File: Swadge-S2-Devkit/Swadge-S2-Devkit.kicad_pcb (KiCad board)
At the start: 2 copper layers, 99.9 x 99.9 mm, 72 parts, among them J1 USB_B_Micro, M1 Motor_DC, Q1 Q_NPN_BEC, Q2 Q_NPN_BEC, SW1 4-1437565-2, SW10 4-1437565-2, SW11 4-1437565-2, SW12 4-1437565-2, SW13 touch-ring-6, SW14 SW_SPDT, SW2 4-1437565-2, SW3 4-1437565-2, SW4 4-1437565-2, SW5 4-1437565-2, SW6 4-1437565-2, SW7 4-1437565-2, SW8 4-1437565-2, SW9 4-1437565-2, U1 ESP32-S2-SOLO, U2 BUS_PCIexpress, U3 AP1117-33, U4 GS321-TR, U5 QMA7981, U6 INGHAi_GSPK2308P-8R0.5W, U7 TFT-1.14, U8 TFT_DISPLAY

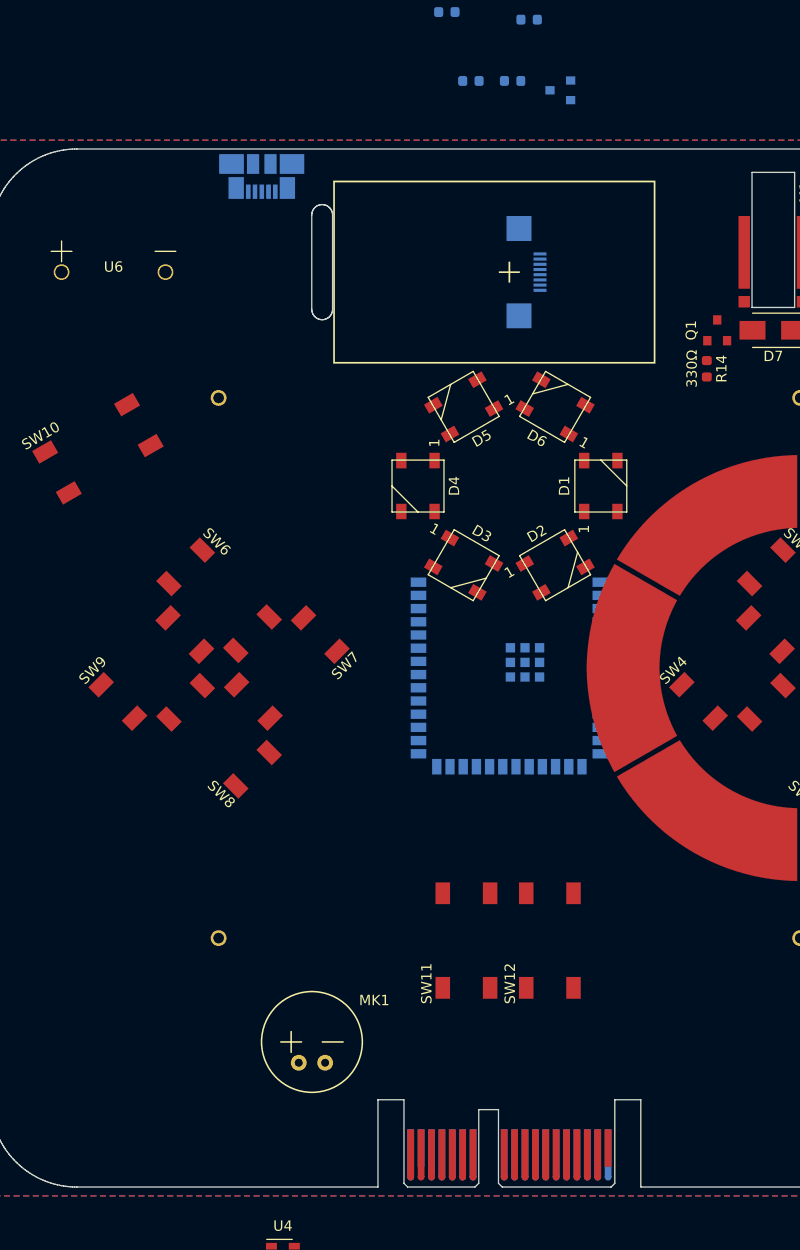
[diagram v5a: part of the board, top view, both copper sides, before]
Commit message: Added diodes to USB, added pin headers, cleaned schematic
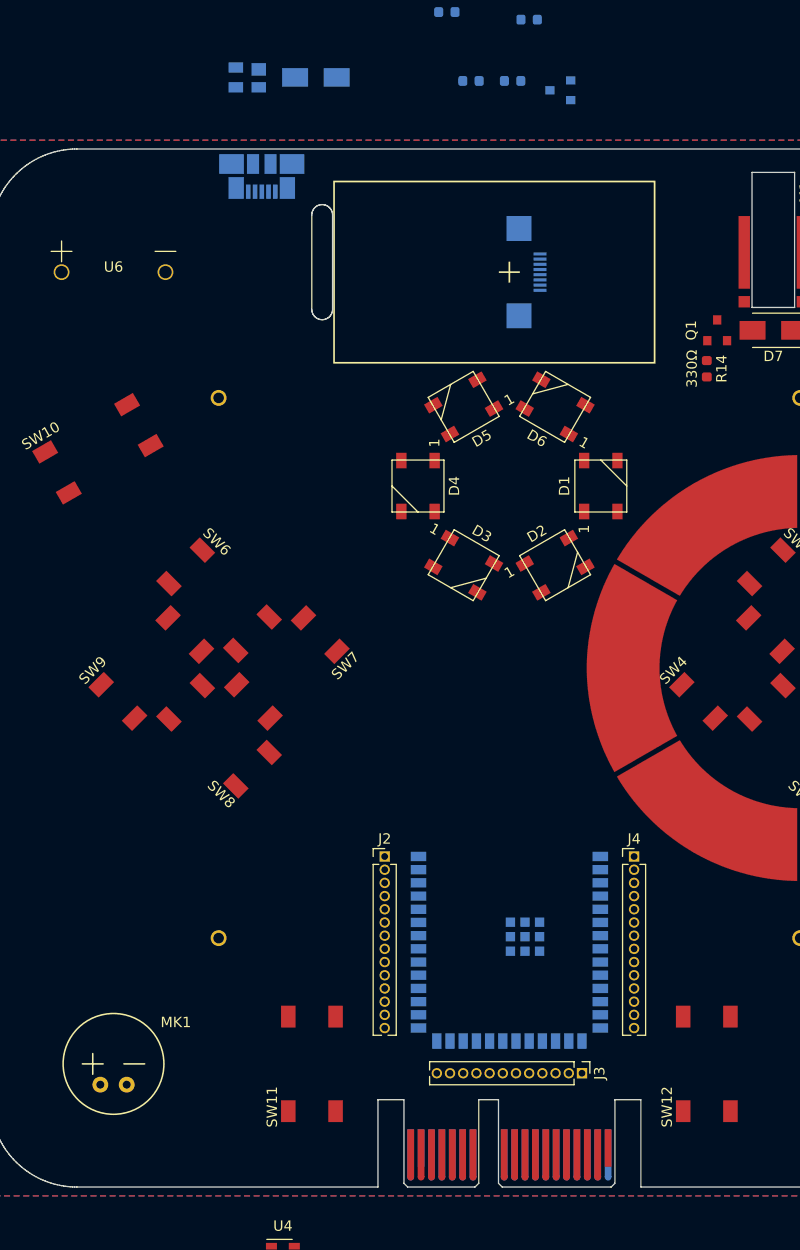
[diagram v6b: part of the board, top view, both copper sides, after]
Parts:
- added D8: SP0503BAHT, Swadge_Parts:SOT-143, B.Cu at (127.2, 44.8)
- added D9: D, Swadge_Parts:D_SMA, B.Cu at (133.8, 44.8)
- added J2: Conn_01x14_Male, Swadge_Parts:PinHeader_1x14_P1.27mm_Vertical, F.Cu at (140.4, 119.7)
- added J3: Conn_01x12_Male, Swadge_Parts:PinHeader_1x12_P1.27mm_Vertical, F.Cu at (159.4, 140.6)
- added J4: Conn_01x14_Male, Swadge_Parts:PinHeader_1x14_P1.27mm_Vertical, F.Cu at (164.4, 119.7)
- moved U1 26.4 mm to (152.4, 128.0)
- moved MK1 19.2 mm to (114.3, 139.7)
- moved SW12 19.2 mm to (171.4, 139.7)
- moved SW11 19.0 mm to (133.4, 139.7)
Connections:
- net Net-(C1-Pad1) renamed EN
- J1 pad 1: +5V -> Net-(D8-Pad4)
- U1 pad 33: unconnected-(U1-Pad33) -> GPIO40
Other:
- outline, holes or cut-outs redrawn

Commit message: Working on devkit, progress.
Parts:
- removed C15: 33μF, Swadge_Parts:C_0603_1608Metric
- removed C16: 10μF, Swadge_Parts:C_0603_1608Metric
- added L2: 100uH, Swadge_Parts:L_0603_1608Metric, F.Cu at (210.9, 96.1)
- added Q3: AP2003_PN_FET, Swadge_Parts:SOT-23-6, F.Cu at (128.2, 66.3)
- added Q4: Q_N_FET, Swadge_Parts:SOT-23, B.Cu at (160.9, 89.1)
- added R18: 680Ω, Swadge_Parts:R_0603_1608Metric, F.Cu at (210.9, 98.6)
- added R19: 680Ω, Swadge_Parts:R_0603_1608Metric, F.Cu at (206.9, 98.7)
- added R20: 680Ω, Swadge_Parts:R_0603_1608Metric, F.Cu at (206.9, 101.2)
- added R21: 0Ω, Swadge_Parts:R_0603_1608Metric, F.Cu at (120.2, 132.3)
- added R22: NP, Swadge_Parts:R_0603_1608Metric, F.Cu at (206.9, 93.7)
- C1, C2, C3, D8, D9, J1, R1, U1: moved to F.Cu
- J2, J4: moved to B.Cu
- J3: value Conn_01x12_Male -> Conn_01x14_Male; footprint Swadge_Parts:PinHeader_1x12_P1.27mm_Vertical -> Swadge_Parts:PinHeader_1x14_P1.27mm_Vertical; moved to B.Cu
- L1: value 10μH -> 2.2uH
- Q1: value Q_NPN_BEC -> Q_N_FET
- Q2: value Q_NPN_BEC -> AP2003_PN_FET; footprint Swadge_Parts:SOT-23 -> Swadge_Parts:SOT-23-6; moved to F.Cu
- R10: value 100Ω -> NP
- R13: value 1Ω -> 33Ω
- R14: value 330Ω -> 33Ω
- R15: value 22Ω -> 680Ω; moved to F.Cu
- R16: value 10kΩ -> 680Ω; moved to F.Cu
- R17: value 1kΩ -> 680Ω; moved to F.Cu
- R2: value 10kΩ -> NP; moved to F.Cu
- R3: value 10kΩ -> NP
- R4: value 10kΩ -> 100Ω; moved to F.Cu
- SW13: footprint Swadge_Parts:touch_six -> Swadge_Parts:Touch_Teeth_5
- moved L1 124.0 mm to (206.9, 96.2)
- moved C14 110.3 mm to (169.8, 77.5), turned to 90 degrees
- moved U5 103.0 mm to (165.7, 75.6), turned to -150 degrees
- moved C13 100.1 mm to (162.7, 79.8), turned to 150 degrees
- moved C7 99.3 mm to (110.0, 117.3)
- moved R11 97.6 mm to (138.3, 64.6), turned to 180 degrees
- moved R12 94.0 mm to (138.3, 66.1), turned to 180 degrees
- moved R16 89.6 mm to (214.9, 96.2), turned to 0 degrees
- moved R15 87.3 mm to (222.2, 92.3), turned to 0 degrees
- moved U3 81.3 mm to (109.9, 123.8), turned to -90 degrees
- moved C6 78.9 mm to (143.6, 121.0), turned to 150 degrees
- moved R17 75.7 mm to (210.9, 93.6), turned to 0 degrees
- moved C5 75.2 mm to (152.0, 135.6), turned to -90 degrees
- moved J2 71.0 mm to (165.4, 53.3), turned to 180 degrees
- moved J4 70.3 mm to (141.4, 53.3), turned to 180 degrees
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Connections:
- C11 pad 1: MIC -> Net-(C11-Pad1)
- D8 pad 2: USB_D- -> Net-(D8-Pad2)
- D8 pad 3: USB_D+ -> Net-(D8-Pad3)
- J1 pad 2: USB_D- -> Net-(D8-Pad2)
- J1 pad 3: USB_D+ -> Net-(D8-Pad3)
- J3 pad 1: TFT_LEDA -> GND
- J3 pad 10: TFT_SCL -> TOUCH_6
- J3 pad 11: TFT_SDA -> TFT_RS
- J3 pad 12: TFT_CS -> TFT_SCL
- J3 pad 2: TFT_RESET -> TFT_LEDA_TRIG
- J3 pad 3: TOUCH_1 -> TFT_LEDA
- J3 pad 4: TOUCH_2 -> TFT_RESET
- J3 pad 5: TOUCH_3 -> TOUCH_1
- J3 pad 6: TOUCH_4 -> TOUCH_2
- J3 pad 7: TOUCH_5 -> TOUCH_3
- J3 pad 8: TOUCH_6 -> TOUCH_4
- J3 pad 9: TFT_RS -> TOUCH_5
- L1 pad 1: SPK -> +3V3
- L1 pad 2: Net-(L1-Pad2) -> DIPRAIL
- Q1 pad 1: Net-(Q1-Pad1) -> MOTOR
- Q2 pad 1: Net-(Q2-Pad1) -> SPK
- Q2 pad 2: Net-(Q2-Pad2) -> DIPRAIL
- Q2 pad 3: Net-(Q2-Pad3) -> SPK
- R13 pad 1: Net-(L1-Pad2) -> USB_D+
- R13 pad 2: Net-(C15-Pad1) -> Net-(D8-Pad3)
- R14 pad 1: Net-(Q1-Pad1) -> USB_D-
- R14 pad 2: MOTOR -> Net-(D8-Pad2)
- R15 pad 1: +3V3 -> Net-(R15-Pad1)
- R15 pad 2: Net-(Q2-Pad3) -> TOUCH_1
- R16 pad 1: +3V3 -> Net-(R16-Pad1)
- R16 pad 2: TFT_LEDA -> TOUCH_2
- R17 pad 1: TFT_LEDA -> Net-(R17-Pad1)
- R17 pad 2: Net-(Q2-Pad1) -> TOUCH_3
- R9 pad 1: MIC -> Net-(C11-Pad1)
- SW13 pad 1: TOUCH_1 -> Net-(R15-Pad1)
- SW13 pad 2: TOUCH_2 -> Net-(R16-Pad1)
- SW13 pad 3: TOUCH_3 -> Net-(R17-Pad1)
- SW13 pad 4: TOUCH_4 -> Net-(R18-Pad1)
- SW13 pad 5: TOUCH_5 -> Net-(R19-Pad1)
- SW13 pad 6: TOUCH_6 -> Net-(R20-Pad1)
- U4 pad 4: MIC -> Net-(C11-Pad1)
- U6 pad 2: GND -> Net-(Q2-Pad4)
- U7 pad 1: Net-(Q2-Pad2) -> TFT_LEDA
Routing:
- net +3V3: track 0.00 -> 10.6 mm
- net EN: track 0.00 -> 6.55 mm
- net SDA: track 0.00 -> 5.62 mm
- net SCL: track 0.00 -> 5.56 mm
- net USB_D-: track 0.00 -> 3.25 mm
- net USB_D+: track 0.00 -> 3.25 mm
- net MIC: track 0.00 -> 3.25 mm
- net TFT_LEDA: track 0.00 -> 3.01 mm

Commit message: Bump rev.
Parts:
- removed R10: NP, Swadge_Parts:R_0603_1608Metric
- removed SW10, SW11, SW12: 4-1437565-2, Swadge_Parts:SW_4-1437565-2
- added BTN1: BLISTER_SILICONE_BUTTON, Swadge_Parts:BTC007_Button_Silicone, F.Cu at (124.6, 87.5)
- L2: footprint Swadge_Parts:L_0603_1608Metric -> Swadge_Parts:L_0805_2012Metric; moved to B.Cu
- Q4: value Q_N_FET -> AP2003_PN_FET; footprint Swadge_Parts:SOT-23 -> Swadge_Parts:SOT-23-6
- R15, R16, R17, R18, R19, R20: moved to B.Cu
- moved SW5 110.3 mm to (109.2, 81.1), turned to 180 degrees
- moved R22 100.4 mm to (117.1, 138.6), turned to 120 degrees
- moved SW1 84.1 mm to (180.3, 121.1)
- moved SW3 84.1 mm to (180.3, 134.1)
- moved SW2 84.1 mm to (186.8, 127.6)
- moved SW4 84.1 mm to (173.8, 127.6)
- moved L1 83.3 mm to (130.4, 63.1), turned to 180 degrees
- moved R3 79.5 mm to (137.5, 61.6), turned to -90 degrees
- moved R15 74.6 mm to (149.0, 77.5), turned to 90 degrees
- moved L2 68.2 mm to (143.3, 87.2), turned to 90 degrees
- moved R16 67.0 mm to (150.6, 77.5), turned to 90 degrees
- moved R18 61.0 mm to (153.6, 77.5), turned to 90 degrees
- moved R17 61.0 mm to (152.1, 77.5), turned to 90 degrees
- moved R19 55.9 mm to (155.1, 77.5), turned to 90 degrees
- moved R20 55.5 mm to (156.7, 77.5), turned to 90 degrees
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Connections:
- J2 pad 10: BTN_10 -> BTN_3
- J2 pad 11: BTN_9 -> TFTATN
- J2 pad 12: BTN_8 -> TFT_CS
- J2 pad 13: BTN_12 -> TFT_RESET
- J2 pad 14: BTN_11 -> BTN_8
- J2 pad 5: TX -> RX
- J2 pad 6: SPK -> SP+
- J2 pad 7: BZR -> SP-
- J2 pad 8: GPIO40 -> BZR
- J3 pad 14: TFT_CS -> TFTATP
- J3 pad 3: TFT_LEDA -> BTN_9
- J3 pad 4: TFT_RESET -> BTN_4
- J4 pad 6: BTN_3 -> SPARE1
- J4 pad 7: BTN_4 -> BLISTER1
- L2 pad 1: TFT_LEDA -> Net-(L2-Pad1)
- L2 pad 2: +3V3 -> TFT_LEDA
- LS1 pad 1: Net-(LS1-Pad1) -> BZR
- Q2 pad 1: SPK -> SP-
- Q2 pad 3: SPK -> SP-
- Q3 pad 1: BZR -> SP+
- Q3 pad 3: BZR -> SP+
- Q4 pad 1: TFT_LEDA_TRIG -> TFTATN
- Q4 pad 2: GND -> +3V3
- Q4 pad 3: TFT_LEDA -> TFTATP
- U1 pad 15: TFT_LEDA -> BTN_9
- U1 pad 16: TFT_RESET -> BTN_4
- U1 pad 26: TFT_CS -> TFTATP
- U1 pad 27: BTN_11 -> BTN_8
- U1 pad 28: BTN_12 -> TFT_RESET
- U1 pad 29: BTN_8 -> TFT_CS
- U1 pad 30: BTN_9 -> TFTATN
- U1 pad 31: BTN_10 -> BTN_3
- U1 pad 33: GPIO40 -> BZR
- U1 pad 34: BZR -> SP-
- U1 pad 35: SPK -> SP+
- U1 pad 6: BTN_3 -> SPARE1
- U1 pad 7: BTN_4 -> BLISTER1
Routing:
- net SDA: track 5.62 -> 0.00 mm
- net SCL: track 5.56 -> 0.00 mm
- net +3V3: track 10.6 -> 5.11 mm
- net USB_D-: track 3.25 -> 0.00 mm
- net USB_D+: track 3.25 -> 0.00 mm
- net MIC: track 3.25 -> 0.00 mm
- net EN: track 6.55 -> 3.30 mm
- net TFT_LEDA: track 3.01 -> 0.00 mm
